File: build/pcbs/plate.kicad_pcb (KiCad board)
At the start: 2 copper layers, 127.2 x 107.5 mm, 21 parts

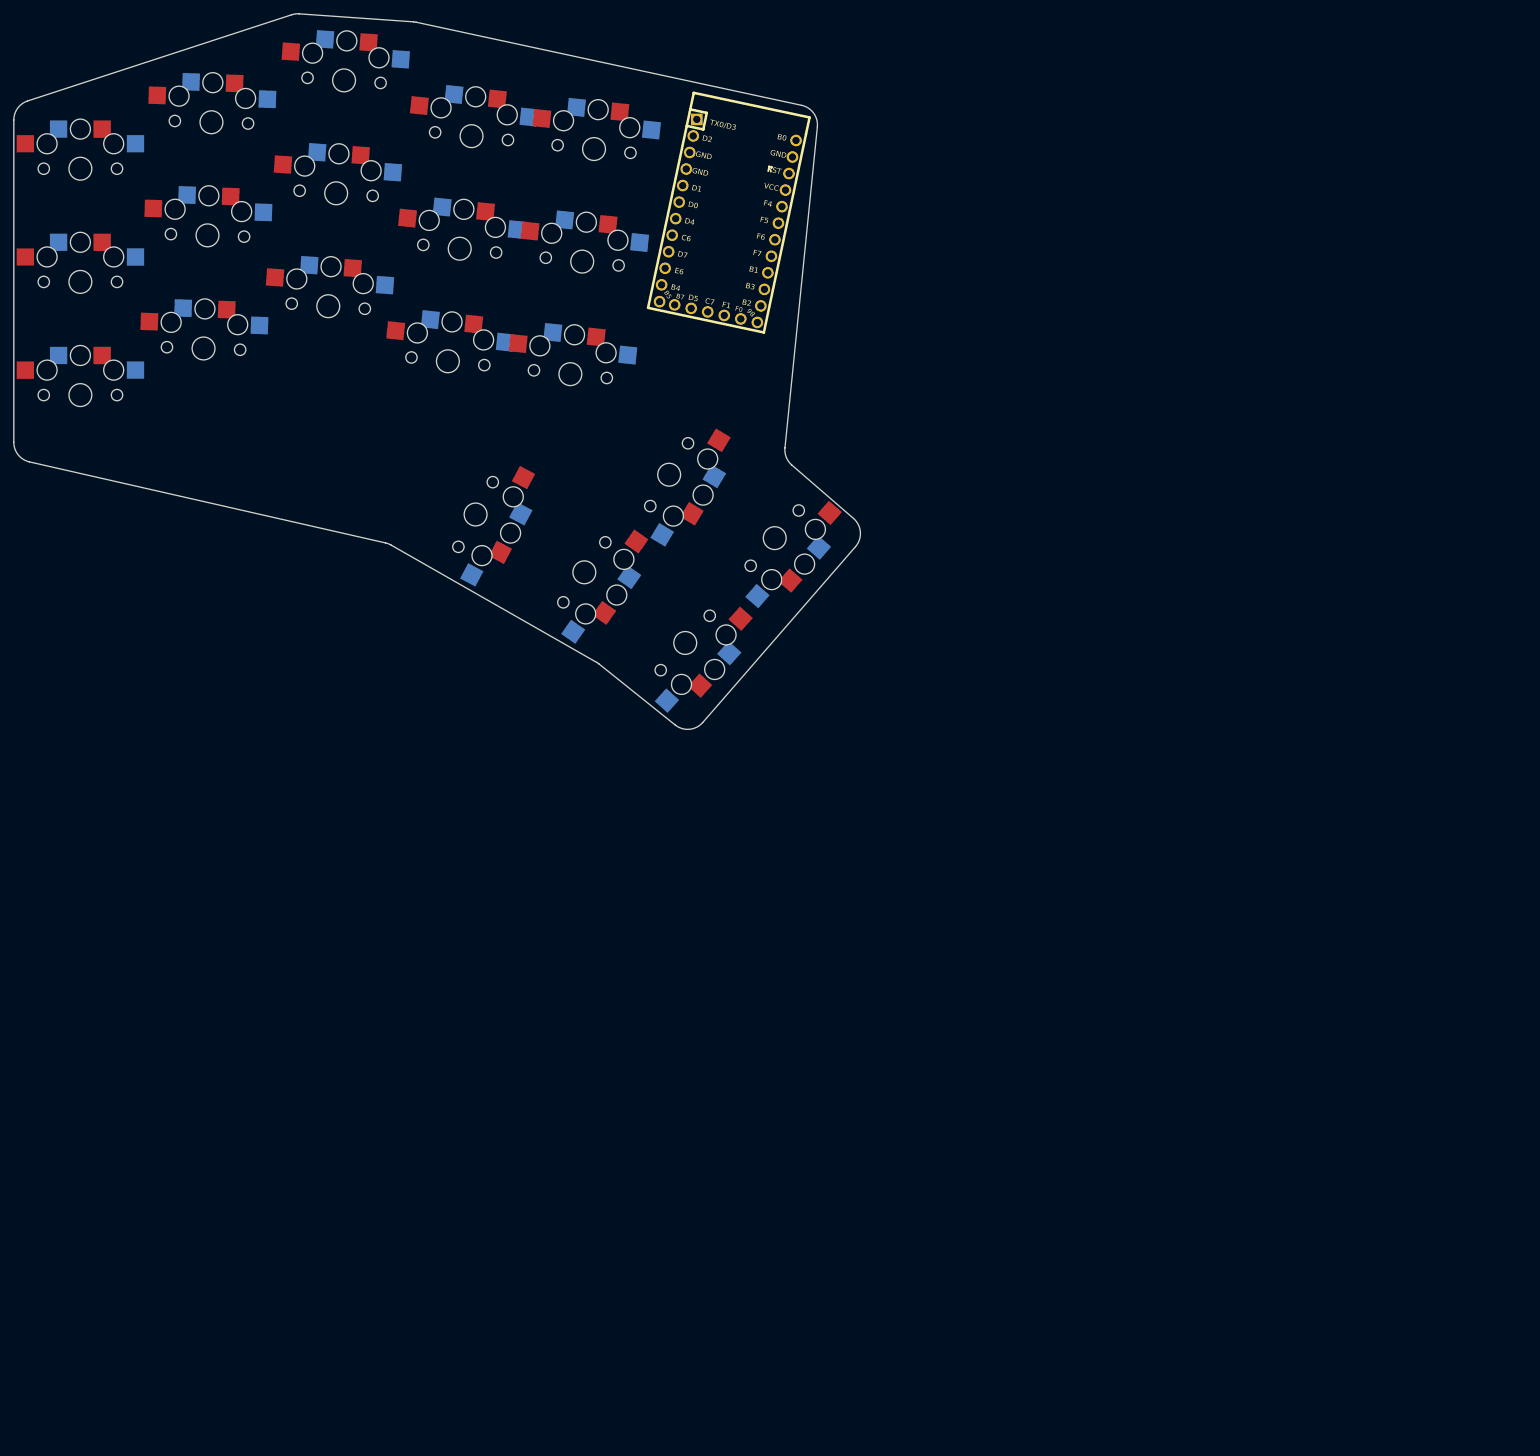
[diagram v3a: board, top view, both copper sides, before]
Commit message: Add nicenano controller
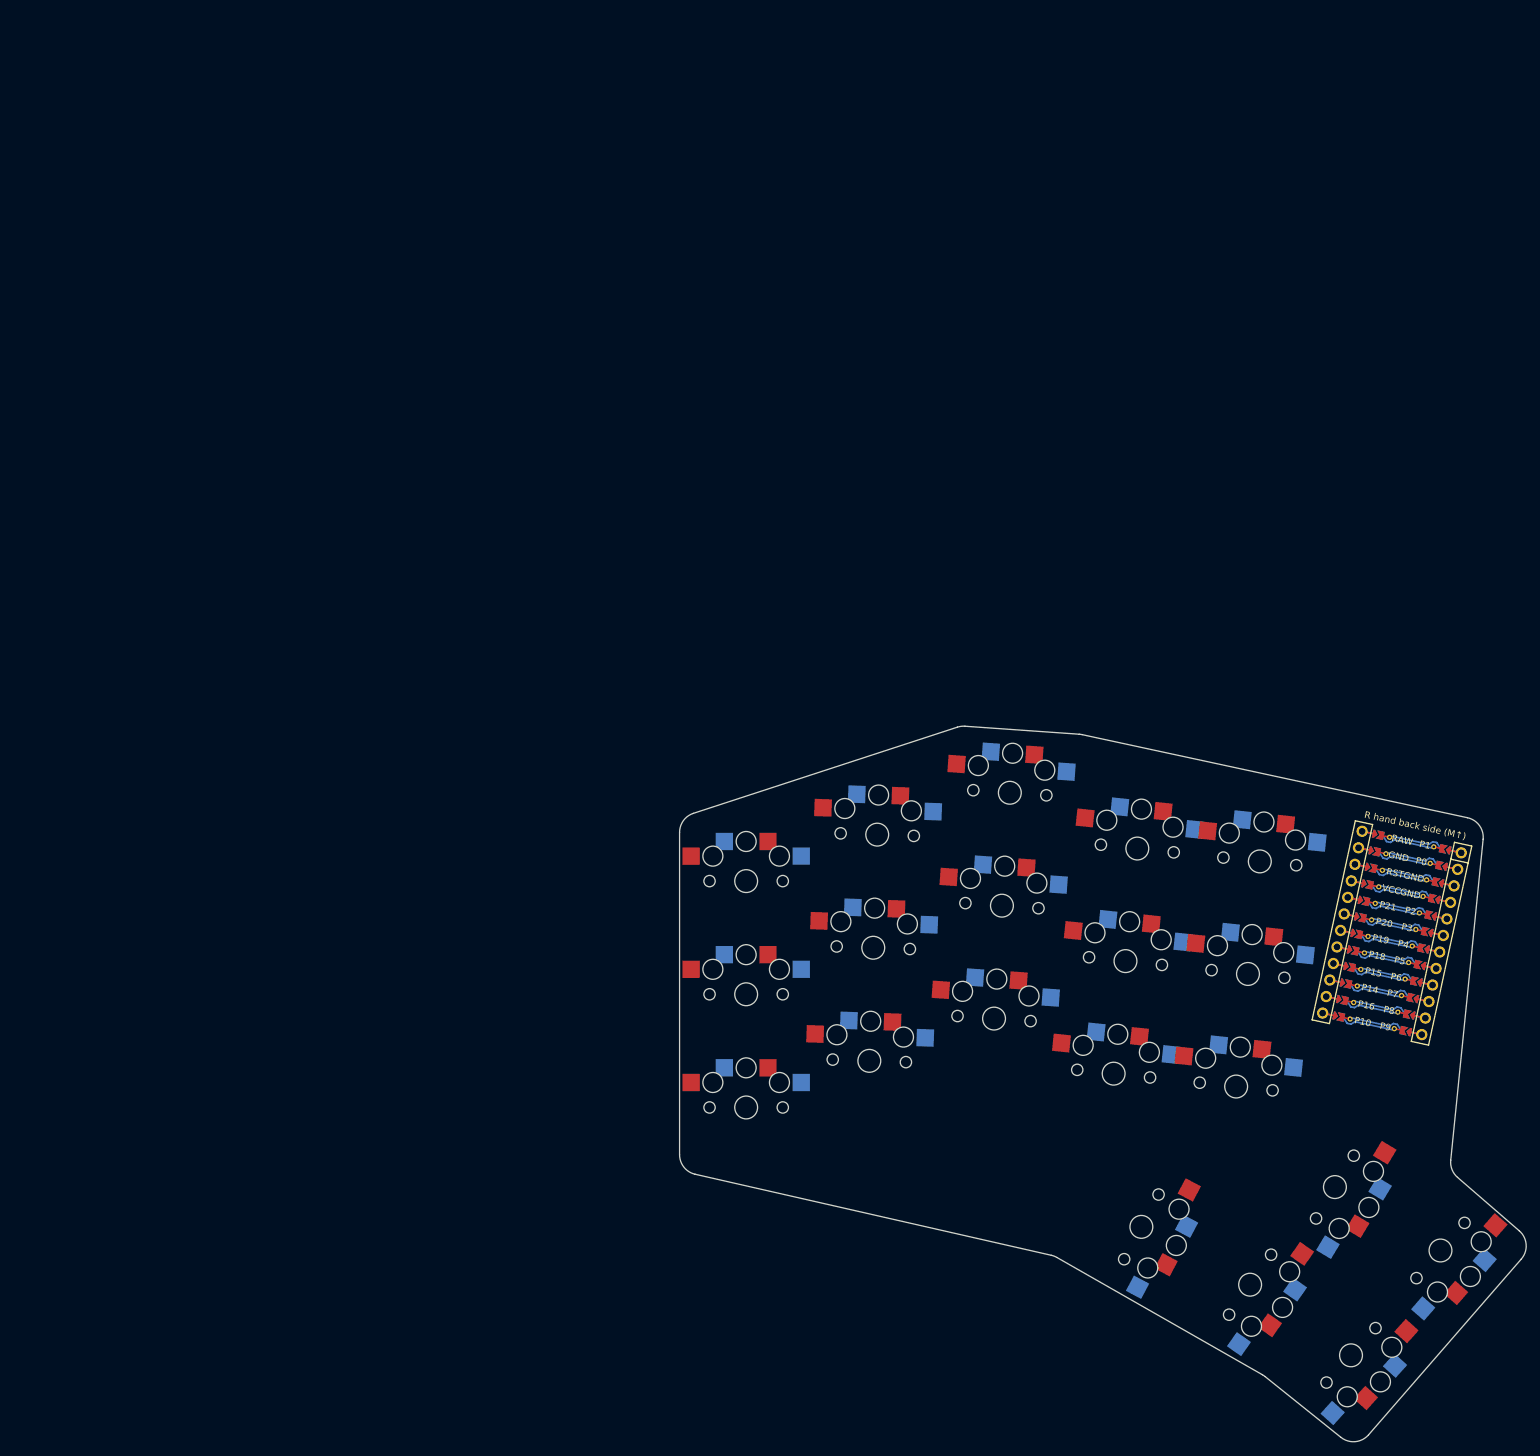
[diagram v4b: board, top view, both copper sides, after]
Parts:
- MCU1: value Elite-C -> (none); footprint Elite-C -> ceoloide:mcu_nice_nano
- moved S12 146.5 mm to (158.8, 61.1)
- moved S9 146.5 mm to (139.6, 52.7)
- moved S1 146.5 mm to (100.0, 100.0)
- moved S11 146.5 mm to (157.0, 78.0)
- moved S13 146.5 mm to (173.6, 96.9)
- moved S14 146.5 mm to (175.4, 80.0)
- moved S15 146.5 mm to (177.2, 63.0)
- moved S17 146.5 mm to (204.3, 121.5)
- moved S18 146.5 mm to (159.4, 117.9)
- moved S2 146.5 mm to (100.0, 83.0)
- moved S3 146.5 mm to (100.0, 66.0)
- moved S4 146.5 mm to (118.5, 93.0)
- moved S5 146.5 mm to (119.1, 76.0)
- moved S6 146.5 mm to (119.7, 59.0)
- moved S7 146.5 mm to (137.2, 86.6)
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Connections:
- net B0 renamed MCU1_24
- net B1 renamed MCU1_16
- net B2 renamed MCU1_14
- net B3 renamed MCU1_15
- net B4 renamed MCU1_11
- net B5 renamed MCU1_12
- net B6 renamed MCU1_13
- net C6 renamed MCU1_8
- net D0 renamed MCU1_6
- net D1 renamed MCU1_5
- net D2 renamed MCU1_2
- net D3 renamed MCU1_1
- net D4 renamed MCU1_7
- net D7 renamed MCU1_9
- net E6 renamed MCU1_10
- net F4 renamed MCU1_20
- net F5 renamed MCU1_19
- net F6 renamed MCU1_18
- net F7 renamed MCU1_17
- net ST renamed MCU1_22
- MCU1 pad 21: VCC -> MCU1_21
- MCU1 pad 23: GND -> MCU1_23
- MCU1 pad 3: GND -> MCU1_3
- MCU1 pad 4: GND -> MCU1_4
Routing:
- net (no net): track 0.00 -> 337.7 mm
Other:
- net class Default removed
